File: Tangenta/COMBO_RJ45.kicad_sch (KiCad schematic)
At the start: 1 part, among them J14 RC01133

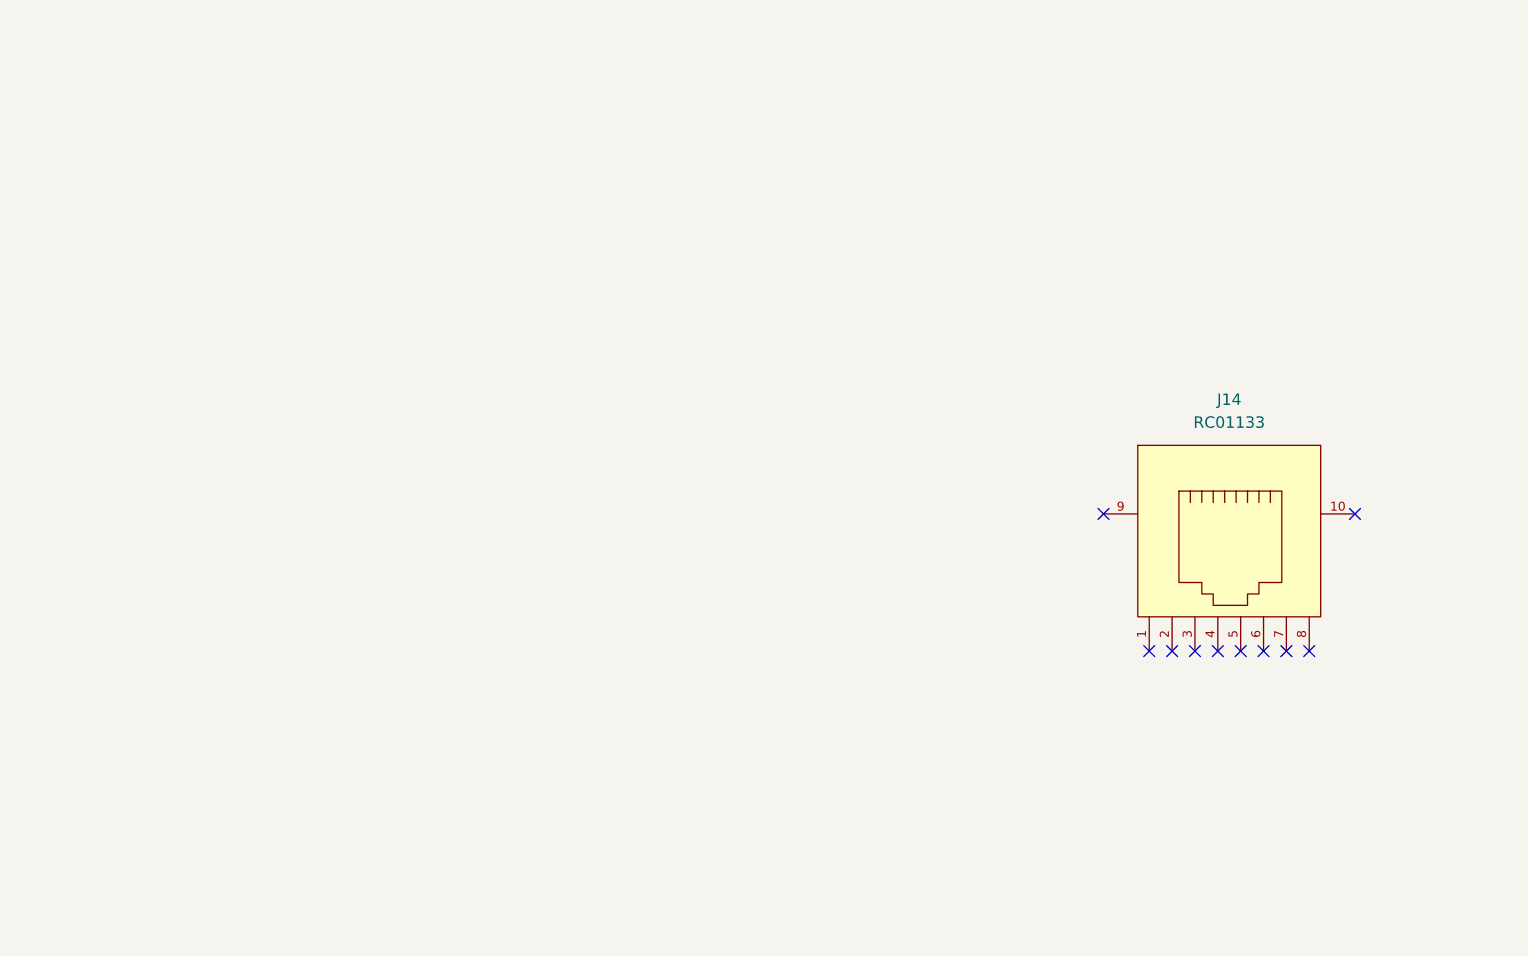
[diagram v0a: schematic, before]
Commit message: Dual RS485 routed, done.
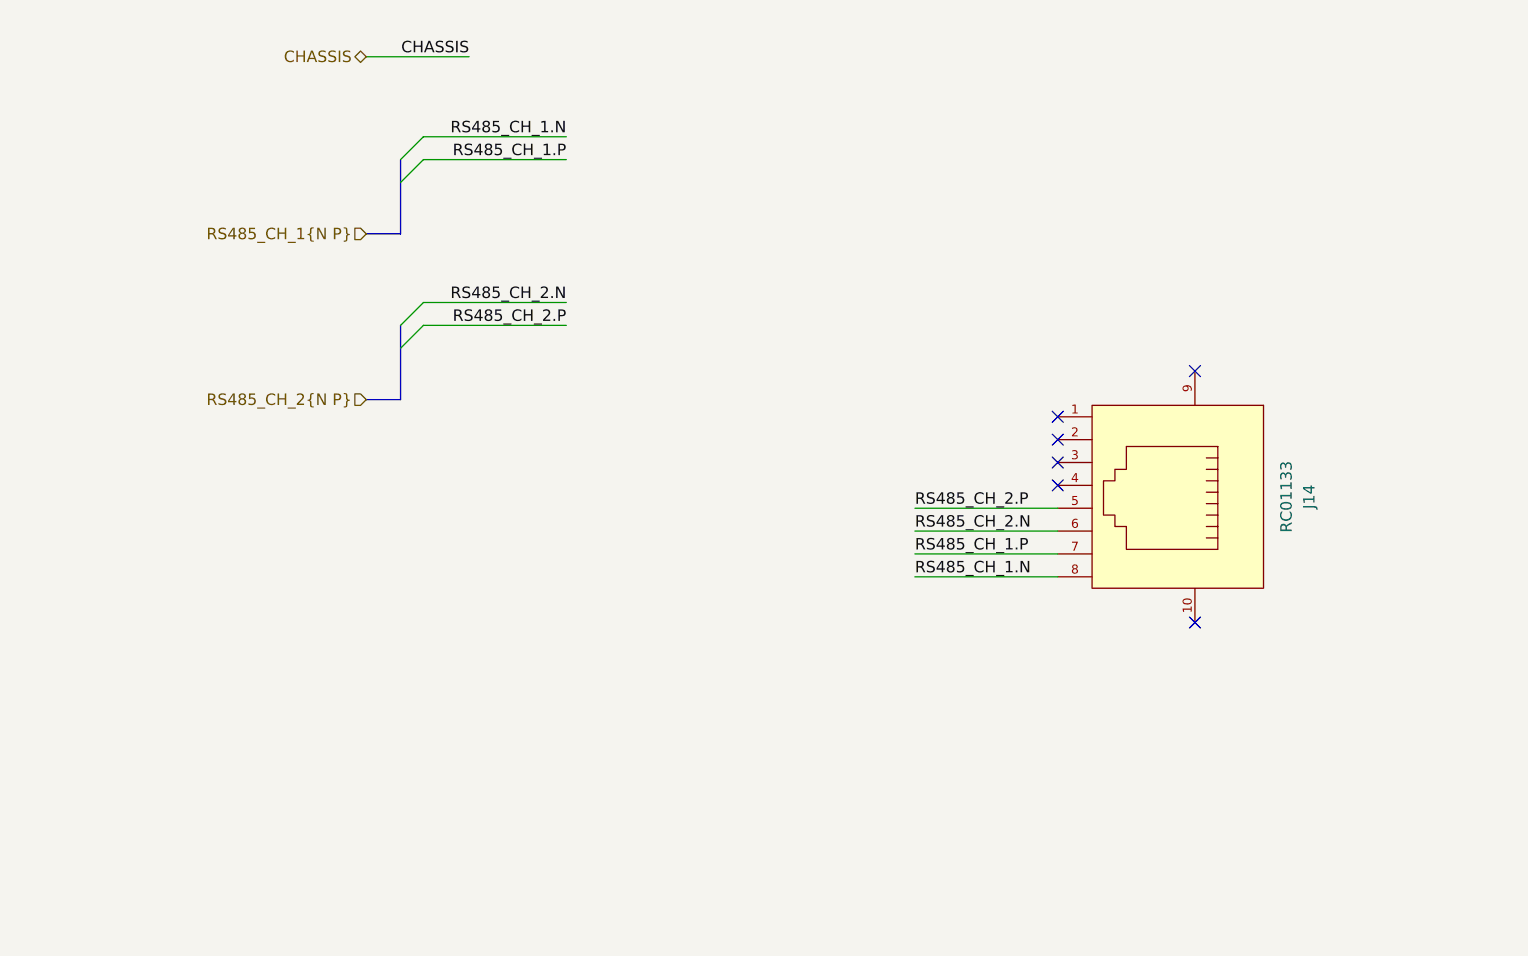
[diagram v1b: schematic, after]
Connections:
- net RS485_CH_2.P: now reaches J14.5
- net RS485_CH_2.N: now reaches J14.6
- net RS485_CH_1.P: now reaches J14.7
- net RS485_CH_1.N: now reaches J14.8
- no-connect marks 10 -> 6
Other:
- moved on the sheet: J14
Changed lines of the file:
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@@
 (kicad_sch (version 20230121) (generator eeschema)
   (paper "A4")
-  (no_connect (at 151.765 96.52))
-  (no_connect (at 146.685 96.52))
-  (no_connect (at 161.925 96.52))
-  (no_connect (at 149.225 96.52))
-  (no_connect (at 169.545 81.28))
-  (no_connect (at 164.465 96.52))
-  (no_connect (at 141.605 81.28))
-  (no_connect (at 156.845 96.52))
-  (no_connect (at 159.385 96.52))
-  (no_connect (at 154.305 96.52))
-  (symbol (lib_id "RJ45_SIMPLE:RC01133") (at 156.845 86.36 0) (unit 1)
+  (no_connect (at 136.525 75.565))
+  (no_connect (at 136.525 70.485))
+  (no_connect (at 136.525 73.025))
+  (no_connect (at 151.765 93.345))
+  (no_connect (at 151.765 65.405))
+  (no_connect (at 136.525 78.105))
+  (bus_entry (at 63.5 62.865) (size 2.54 -2.54)
+    (stroke (width 0) (type default))
+  )
+  (bus_entry (at 63.5 60.325) (size 2.54 -2.54)
+    (stroke (width 0) (type default))
+  )
+  (bus_entry (at 63.5 41.91) (size 2.54 -2.54)
+    (stroke (width 0) (type default))
+  )
+  (bus_entry (at 63.5 44.45) (size 2.54 -2.54)
+    (stroke (width 0) (type default))
+  )
+  (wire (pts (xy 81.915 57.785) (xy 66.04 57.785))
+    (stroke (width 0) (type default))
+  )
+  (bus (pts (xy 63.5 50.165) (xy 59.69 50.165))
+    (stroke (width 0) (type default))
+  )
+  (wire (pts (xy 81.915 60.325) (xy 66.04 60.325))
+    (stroke (width 0) (type default))
+  )
+  (bus (pts (xy 63.5 62.865) (xy 63.5 68.58))
+    (stroke (width 0) (type default))
+  )
+  (bus (pts (xy 63.5 60.325) (xy 63.5 62.865))
+    (stroke (width 0) (type default))
+  )
+  (wire (pts (xy 136.525 85.725) (xy 120.65 85.725))
+    (stroke (width 0) (type default))
+  )
+  (wire (pts (xy 59.69 30.48) (xy 71.12 30.48))
+    (stroke (width 0) (type default))
+  )
+  (bus (pts (xy 63.5 41.91) (xy 63.5 44.45))
+    (stroke (width 0) (type default))
+  )
+  (wire (pts (xy 136.525 88.265) (xy 120.65 88.265))
+    (stroke (width 0) (type default))
+  )
+  (wire (pts (xy 81.915 39.37) (xy 66.04 39.37))
+    (stroke (width 0) (type default))
+  )
+  (bus (pts (xy 63.5 68.58) (xy 59.69 68.58))
+    (stroke (width 0) (type default))
+  )
+  (wire (pts (xy 136.525 83.185) (xy 120.65 83.185))
+    (stroke (width 0) (type default))
+  )
+  (bus (pts (xy 63.5 44.45) (xy 63.5 50.165))
+    (stroke (width 0) (type default))
+  )
+  (wire (pts (xy 81.915 41.91) (xy 66.04 41.91))
+    (stroke (width 0) (type default))
+  )
+  (wire (pts (xy 136.525 80.645) (xy 120.65 80.645))
+    (stroke (width 0) (type default))
+  )
+  (label "RS485_CH_1.N" (at 120.65 88.265 0) (fields_autoplaced)
+    (effects (font (size 1.27 1.27)) (justify left bottom))
+  )
+  (label "RS485_CH_1.N" (at 81.915 39.37 180) (fields_autoplaced)
+    (effects (font (size 1.27 1.27)) (justify right bottom))
+  )
+  (label "RS485_CH_2.P" (at 81.915 60.325 180) (fields_autoplaced)
+    (effects (font (size 1.27 1.27)) (justify right bottom))
+  )
+  (label "RS485_CH_1.P" (at 81.915 41.91 180) (fields_autoplaced)
+    (effects (font (size 1.27 1.27)) (justify right bottom))
+  )
+  (label "RS485_CH_2.N" (at 120.65 83.185 0) (fields_autoplaced)
+    (effects (font (size 1.27 1.27)) (justify left bottom))
+  )
+  (label "CHASSIS" (at 71.12 30.48 180) (fields_autoplaced)
+    (effects (font (size 1.27 1.27)) (justify right bottom))
+  )
+  (label "RS485_CH_2.P" (at 120.65 80.645 0) (fields_autoplaced)
+    (effects (font (size 1.27 1.27)) (justify left bottom))
+  )
+  (label "RS485_CH_1.P" (at 120.65 85.725 0) (fields_autoplaced)
+    (effects (font (size 1.27 1.27)) (justify left bottom))
+  )
+  (label "RS485_CH_2.N" (at 81.915 57.785 180) (fields_autoplaced)
+    (effects (font (size 1.27 1.27)) (justify right bottom))
+  )
+  (hierarchical_label "RS485_CH_1{N P}" (shape input) (at 59.69 50.165 180) (fields_autoplaced)
+    (effects (font (size 1.27 1.27)) (justify right))
+  )
+  (hierarchical_label "RS485_CH_2{N P}" (shape input) (at 59.69 68.58 180) (fields_autoplaced)
+    (effects (font (size 1.27 1.27)) (justify right))
+  )
+  (hierarchical_label "CHASSIS" (shape bidirectional) (at 59.69 30.48 180) (fields_autoplaced)
+    (effects (font (size 1.27 1.27)) (justify right))
+  )
+  (symbol (lib_id "RJ45_SIMPLE:RC01133") (at 146.685 80.645 270) (unit 1)
     (in_bom yes) (on_board yes) (dnp no) (fields_autoplaced)
-    (property "Reference" "J14" (at 155.575 68.58 0)
+    (property "Reference" "J14" (at 164.465 79.375 0)
       (effects (font (size 1.27 1.27)))
     )
-    (property "Value" "RC01133" (at 155.575 71.12 0)
+    (property "Value" "RC01133" (at 161.925 79.375 0)
       (effects (font (size 1.27 1.27)))
     )
-    (property "Footprint" "RJ45_SIMPLE:RJ45_SIMPLE" (at 158.115 111.76 0)
+    (property "Footprint" "RJ45_SIMPLE:RJ45_SIMPLE" (at 121.285 81.915 0)
       (effects (font (size 1.27 1.27) italic) hide)
     )
-    (property "Datasheet" "https://atta.szlcsc.com/upload/public/pdf/source/20200728/C708616_F79F0C1A8A5D9701E7B7144C9F29FA5C.pdf" (at 145.415 114.3 0)
+    (property "Datasheet" "https://atta.szlcsc.com/upload/public/pdf/source/20200728/C708616_F79F0C1A8A5D9701E7B7144C9F29FA5C.pdf" (at 118.745 69.215 0)
       (effects (font (size 1.27 1.27)) (justify left) hide)
     )
-    (property "LCSC" "C708616" (at 150.495 109.22 0)
+    (property "LCSC" "C708616" (at 123.825 74.295 0)
       (effects (font (size 1.27 1.27)) hide)
     )

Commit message: Removing the old RS485 non-isolated transceivers.
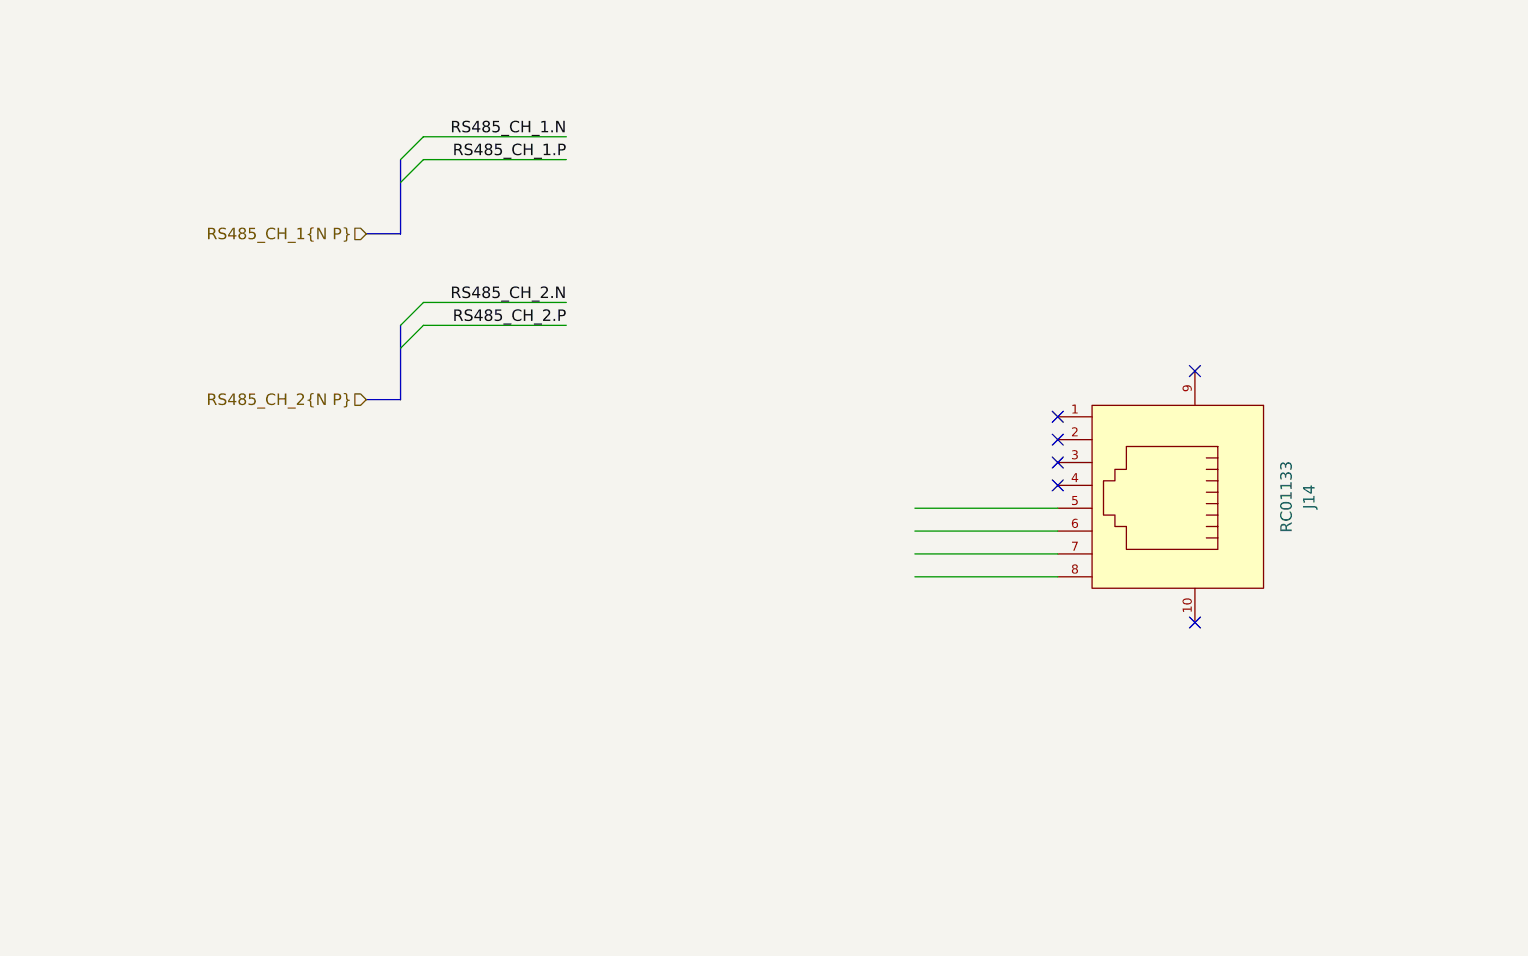
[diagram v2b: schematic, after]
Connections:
- net RS485_CH_1.N: no longer J14.8
- net RS485_CH_1.P: no longer J14.7
- net RS485_CH_2.N: no longer J14.6
- net RS485_CH_2.P: no longer J14.5
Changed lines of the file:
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@@
-    (stroke (width 0) (type default))
-  )
-  (wire (pts (xy 59.69 30.48) (xy 71.12 30.48))
     (stroke (width 0) (type default))
   )
@@
     (stroke (width 0) (type default))
   )
-  (label "RS485_CH_1.N" (at 120.65 88.265 0) (fields_autoplaced)
-    (effects (font (size 1.27 1.27)) (justify left bottom))
-  )
   (label "RS485_CH_1.N" (at 81.915 39.37 180) (fields_autoplaced)
     (effects (font (size 1.27 1.27)) (justify right bottom))
@@
   (label "RS485_CH_1.P" (at 81.915 41.91 180) (fields_autoplaced)
     (effects (font (size 1.27 1.27)) (justify right bottom))
-  )
-  (label "RS485_CH_2.N" (at 120.65 83.185 0) (fields_autoplaced)
-    (effects (font (size 1.27 1.27)) (justify left bottom))
-  )
-  (label "CHASSIS" (at 71.12 30.48 180) (fields_autoplaced)
-    (effects (font (size 1.27 1.27)) (justify right bottom))
-  )
-  (label "RS485_CH_2.P" (at 120.65 80.645 0) (fields_autoplaced)
-    (effects (font (size 1.27 1.27)) (justify left bottom))
-  )
-  (label "RS485_CH_1.P" (at 120.65 85.725 0) (fields_autoplaced)
-    (effects (font (size 1.27 1.27)) (justify left bottom))
   )
   (label "RS485_CH_2.N" (at 81.915 57.785 180) (fields_autoplaced)
@@
     (effects (font (size 1.27 1.27)) (justify right))
   )
-  (hierarchical_label "CHASSIS" (shape bidirectional) (at 59.69 30.48 180) (fields_autoplaced)
-    (effects (font (size 1.27 1.27)) (justify right))
-  )

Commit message: ...
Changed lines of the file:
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@@
   (no_connect (at 151.765 65.405))
   (no_connect (at 136.525 78.105))
-  (bus_entry (at 63.5 62.865) (size 2.54 -2.54)
-    (stroke (width 0) (type default))
-  )
-  (bus_entry (at 63.5 60.325) (size 2.54 -2.54)
-    (stroke (width 0) (type default))
-  )
-  (bus_entry (at 63.5 41.91) (size 2.54 -2.54)
-    (stroke (width 0) (type default))
-  )
-  (bus_entry (at 63.5 44.45) (size 2.54 -2.54)
-    (stroke (width 0) (type default))
-  )
-  (wire (pts (xy 81.915 57.785) (xy 66.04 57.785))
-    (stroke (width 0) (type default))
-  )
-  (bus (pts (xy 63.5 50.165) (xy 59.69 50.165))
-    (stroke (width 0) (type default))
-  )
-  (wire (pts (xy 81.915 60.325) (xy 66.04 60.325))
-    (stroke (width 0) (type default))
-  )
-  (bus (pts (xy 63.5 62.865) (xy 63.5 68.58))
-    (stroke (width 0) (type default))
-  )
-  (bus (pts (xy 63.5 60.325) (xy 63.5 62.865))
-    (stroke (width 0) (type default))
-  )
   (wire (pts (xy 136.525 85.725) (xy 120.65 85.725))
-    (stroke (width 0) (type default))
-  )
-  (bus (pts (xy 63.5 41.91) (xy 63.5 44.45))
     (stroke (width 0) (type default))
   )
@@
     (stroke (width 0) (type default))
   )
-  (wire (pts (xy 81.915 39.37) (xy 66.04 39.37))
-    (stroke (width 0) (type default))
-  )
-  (bus (pts (xy 63.5 68.58) (xy 59.69 68.58))
-    (stroke (width 0) (type default))
-  )
   (wire (pts (xy 136.525 83.185) (xy 120.65 83.185))
-    (stroke (width 0) (type default))
-  )
-  (bus (pts (xy 63.5 44.45) (xy 63.5 50.165))
-    (stroke (width 0) (type default))
-  )
-  (wire (pts (xy 81.915 41.91) (xy 66.04 41.91))
     (stroke (width 0) (type default))
   )
@@
     (stroke (width 0) (type default))
   )
-  (label "RS485_CH_1.N" (at 81.915 39.37 180) (fields_autoplaced)
-    (effects (font (size 1.27 1.27)) (justify right bottom))
-  )
-  (label "RS485_CH_2.P" (at 81.915 60.325 180) (fields_autoplaced)
-    (effects (font (size 1.27 1.27)) (justify right bottom))
-  )
-  (label "RS485_CH_1.P" (at 81.915 41.91 180) (fields_autoplaced)
-    (effects (font (size 1.27 1.27)) (justify right bottom))
-  )
-  (label "RS485_CH_2.N" (at 81.915 57.785 180) (fields_autoplaced)
-    (effects (font (size 1.27 1.27)) (justify right bottom))
-  )
-  (hierarchical_label "RS485_CH_1{N P}" (shape input) (at 59.69 50.165 180) (fields_autoplaced)
-    (effects (font (size 1.27 1.27)) (justify right))
-  )
-  (hierarchical_label "RS485_CH_2{N P}" (shape input) (at 59.69 68.58 180) (fields_autoplaced)
-    (effects (font (size 1.27 1.27)) (justify right))
-  )
   (symbol (lib_id "RJ45_SIMPLE:RC01133") (at 146.685 80.645 270) (unit 1)

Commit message: ...
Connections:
- net RS.R_N: now reaches J14.5
- net RS.R_P: now reaches J14.6
- net RS.D_P: now reaches J14.7
- net RS.D_N: now reaches J14.8
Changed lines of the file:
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@@
   (no_connect (at 151.765 65.405))
   (no_connect (at 136.525 78.105))
+  (bus_entry (at 50.8 31.115) (size 2.54 -2.54)
+    (stroke (width 0) (type default))
+  )
+  (bus_entry (at 50.8 33.655) (size 2.54 -2.54)
+    (stroke (width 0) (type default))
+  )
+  (bus_entry (at 50.8 38.735) (size 2.54 -2.54)
+    (stroke (width 0) (type default))
+  )
+  (bus_entry (at 50.8 36.195) (size 2.54 -2.54)
+    (stroke (width 0) (type default))
+  )
+  (wire (pts (xy 53.34 36.195) (xy 71.755 36.195))
+    (stroke (width 0) (type default))
+  )
+  (wire (pts (xy 53.34 28.575) (xy 71.755 28.575))
+    (stroke (width 0) (type default))
+  )
+  (wire (pts (xy 53.34 33.655) (xy 71.755 33.655))
+    (stroke (width 0) (type default))
+  )
+  (bus (pts (xy 50.8 33.655) (xy 50.8 31.115))
+    (stroke (width 0) (type default))
+  )
+  (bus (pts (xy 50.8 36.195) (xy 50.8 38.735))
+    (stroke (width 0) (type default))
+  )
   (wire (pts (xy 136.525 85.725) (xy 120.65 85.725))
+    (stroke (width 0) (type default))
+  )
+  (bus (pts (xy 50.8 44.45) (xy 46.99 44.45))
     (stroke (width 0) (type default))
   )
@@
     (stroke (width 0) (type default))
   )
+  (bus (pts (xy 50.8 33.655) (xy 50.8 36.195))
+    (stroke (width 0) (type default))
+  )
+  (bus (pts (xy 50.8 38.735) (xy 50.8 44.45))
+    (stroke (width 0) (type default))
+  )
   (wire (pts (xy 136.525 83.185) (xy 120.65 83.185))
+    (stroke (width 0) (type default))
+  )
+  (wire (pts (xy 53.34 31.115) (xy 71.755 31.115))
     (stroke (width 0) (type default))
   )
@@
     (stroke (width 0) (type default))
   )
+  (label "RS.R_N" (at 120.65 80.645 0) (fields_autoplaced)
+    (effects (font (size 1.27 1.27)) (justify left bottom))
+  )
+  (label "RS.R_P" (at 71.755 31.115 180) (fields_autoplaced)
+    (effects (font (size 1.27 1.27)) (justify right bottom))
+  )
+  (label "RS.D_N" (at 71.755 33.655 180) (fields_autoplaced)
+    (effects (font (size 1.27 1.27)) (justify right bottom))
+  )
+  (label "RS.D_P" (at 71.755 36.195 180) (fields_autoplaced)
+    (effects (font (size 1.27 1.27)) (justify right bottom))
+  )
+  (label "RS.R_N" (at 71.755 28.575 180) (fields_autoplaced)
+    (effects (font (size 1.27 1.27)) (justify right bottom))
+  )
+  (label "RS.R_P" (at 120.65 83.185 0) (fields_autoplaced)
+    (effects (font (size 1.27 1.27)) (justify left bottom))
+  )
+  (label "RS.D_N" (at 120.65 88.265 0) (fields_autoplaced)
+    (effects (font (size 1.27 1.27)) (justify left bottom))
+  )
+  (label "RS.D_P" (at 120.65 85.725 0) (fields_autoplaced)
+    (effects (font (size 1.27 1.27)) (justify left bottom))
+  )
+  (hierarchical_label "RS{R_N R_P D_N D_P}" (shape input) (at 46.99 44.45 180) (fields_autoplaced)
+    (effects (font (size 1.27 1.27)) (justify right))
+  )
   (symbol (lib_id "RJ45_SIMPLE:RC01133") (at 146.685 80.645 270) (unit 1)
